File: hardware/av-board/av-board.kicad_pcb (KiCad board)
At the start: 6 copper layers, 94.6 x 69.4 mm, 234 parts, among them J1 RCA Y, J10 2x20 socket, J2 RCA Pb, J3 RCA Pr, J4 RCA L, J5 RCA R, J6 HDMI-001, J9 2x20 socket, SW1 TS-1187A-B-A-B, SW2 TS-1187A-B-A-B, U1 ADV7842KBCZ-5, U10 TPD4E05U06DQAR, U2 ADV7511KSTZ, U3 PCM1808PWR, U4 TLV62569DBVR, U5 TPS7A7001DDAR, U6 TPS7A7001DDAR, U7 TPS7A7001DDAR, U8 TPD4E05U06DQAR, U9 TPD4E05U06DQAR, Y1 28.63636MHz 20pF

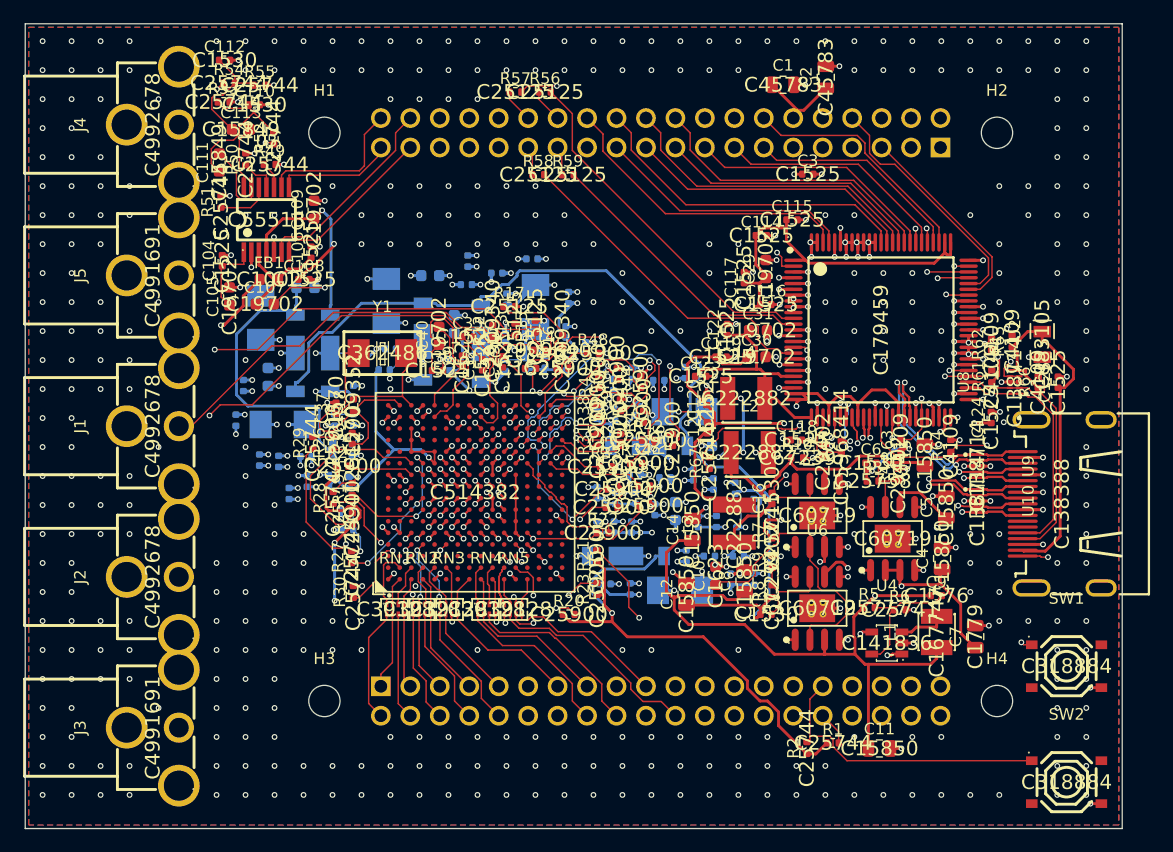
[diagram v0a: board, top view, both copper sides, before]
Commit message: Ready to order: silkscreen, 0.2 mm TMDS on the outer layers, fab outputs
- Silkscreen (gen_pcb.py silkscreen(), also on a routed board with --silk): designators only for
  ICs, connectors, filters, inductors, crystal, buttons and holes, each moved to the first spot
  clear of copper and other text (above, below, beside, on the body) or hidden; the passives' and
  every other field (values, LCSC numbers, which KiCad had put on the silkscreen) hidden. Labels
  Y/Pb/Pr/L/R by the jacks, HDMI, and the board's name. No text over copper; what DRC still lists
  is footprint outline graphics.
- TMDS: CK and D1's mazeroute segments redone at the class's 0.2 mm on F/B only (they were
  0.127 mm, mostly on In2); all four pairs now 0.2 mm, skew at most 5.2 mm (CK, 35 ps). Outer
  layers on JLC06161H-7628B: about 68 R single-ended, 103 R differential at the 0.15 mm gap.
- mazeroute.py: MAZE_LAYERS/MAZE_WIDTH, paths pulled into straight segments.
- fab/: Gerber + drill zip, BOM (47 lines), CPL (229 parts, 83 on the bottom); README "Ordering
  at JLCPCB" for what the files do not say (stack-up, impedance, two-sided assembly).
- A pcbnew pitfall, again: items removed from a board must stay referenced, or later calls
  return untyped objects (silkscreen() re-runs).

DRC: no errors.

Co-Authored-By: Claude Opus 5.5 <noreply@anthropic.com>
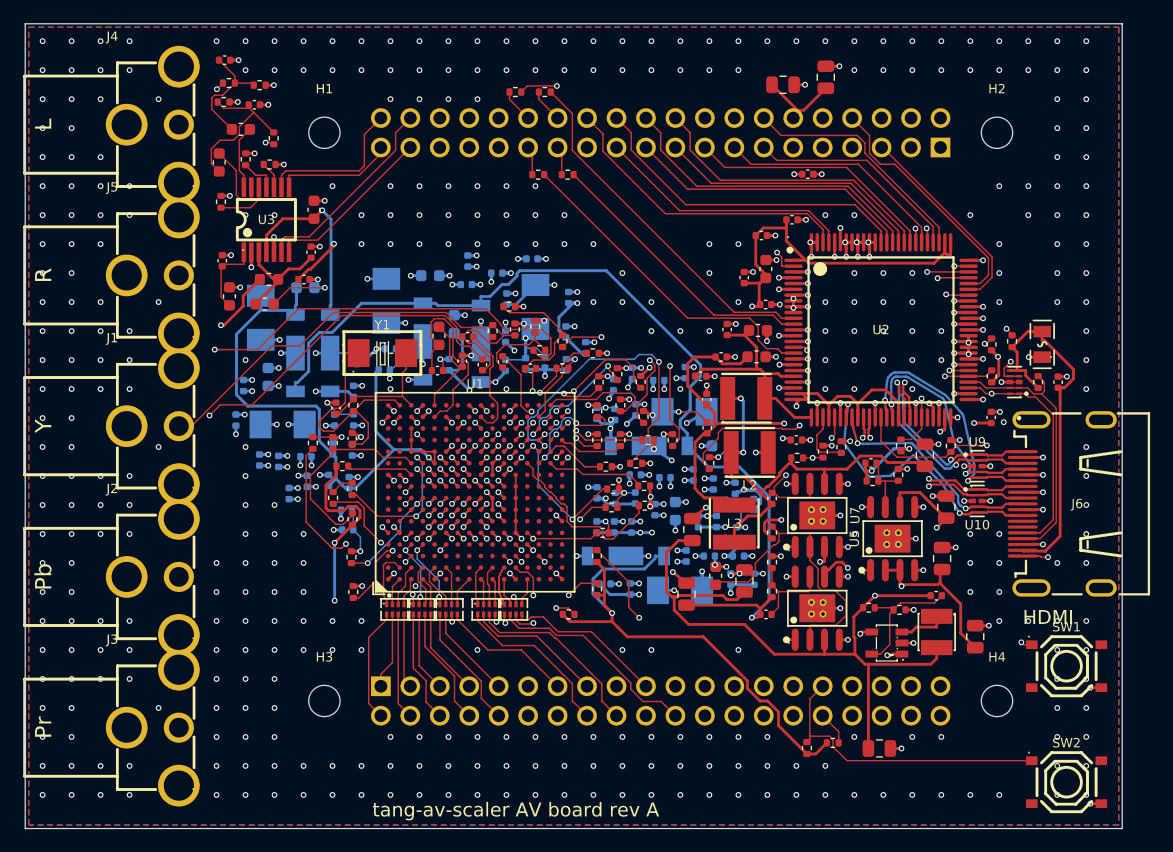
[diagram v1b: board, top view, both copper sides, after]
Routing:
- net TMDS_D1_P: track 14.4 -> 20.6 mm
- net TMDS_D1_N: track 17.6 -> 22.4 mm
- net TMDS_CK_N: track 22.8 -> 24.7 mm, vias 3 -> 2
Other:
- board text added: "HDMI"
- board text added: "L"
- board text added: "Pb"
- board text added: "Pr"
- board text added: "R"
- board text added: "Y"
- board text added: "tang-av-scaler AV board rev A"
